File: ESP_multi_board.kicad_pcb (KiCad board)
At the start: 2 copper layers, 23 parts, among them P101 CONN_01X02, P102 CONN_01X06, P103 CONN_01X02, P104 CONN_01X06, P105 CONN_01X12, P106 CONN_01X03, P107 JUMPER1, P108 CONN_I2C_MPU6050, P109 CONN_01X03, P110 CONN_01X03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

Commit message: pendiente de enrutar, TODO: incluir diodos baterias, meditar los jumpers
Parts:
- moved P107 68.6 mm to (118.1, 71.1)
- moved P112 44.6 mm to (113.0, 94.0), turned to 0 degrees
- moved U1 38.6 mm to (134.6, 82.5)
- moved P110 31.4 mm to (168.9, 90.2), turned to 90 degrees
- moved P109 31.4 mm to (165.1, 95.2), turned to 180 degrees
- moved R104 16.9 mm to (160.0, 88.9), turned to 270 degrees
- moved C1 16.6 mm to (154.9, 88.9), turned to 180 degrees
- moved P103 13.1 mm to (151.1, 86.4), turned to 180 degrees
- moved U101 10.8 mm to (154.9, 97.8)
- moved C2 8.98 mm to (154.9, 108.0), turned to 180 degrees
- moved P104 8.52 mm to (194.3, 90.2)
- moved P105 8.13 mm to (146.1, 104.1)
- moved U103 5.68 mm to (125.7, 96.5)
- moved P101 5.24 mm to (157.5, 83.8)
- moved P111 5.24 mm to (190.5, 104.1)
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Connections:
- U103 pad 10: Net-(P105-Pad3) -> Net-(P105-Pad2)
- U103 pad 11: Net-(P105-Pad2) -> Net-(P105-Pad3)
- U103 pad 12: Net-(P105-Pad1) -> Net-(P105-Pad4)
- U103 pad 9: Net-(P105-Pad4) -> Net-(P105-Pad1)
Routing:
- net VDD: track 54.9 -> 11.8 mm
- net Net-(P111-Pad3): track 31.2 -> 0.00 mm
- net Net-(P111-Pad8): track 18.3 -> 0.00 mm
- net Net-(P111-Pad7): track 17.7 -> 0.00 mm
- net Net-(P111-Pad6): track 17.2 -> 0.00 mm
- net Net-(P111-Pad5): track 16.7 -> 0.00 mm
- net Net-(P111-Pad4): track 16.1 -> 0.00 mm
- net ENC2_B: track 13.3 -> 0.00 mm

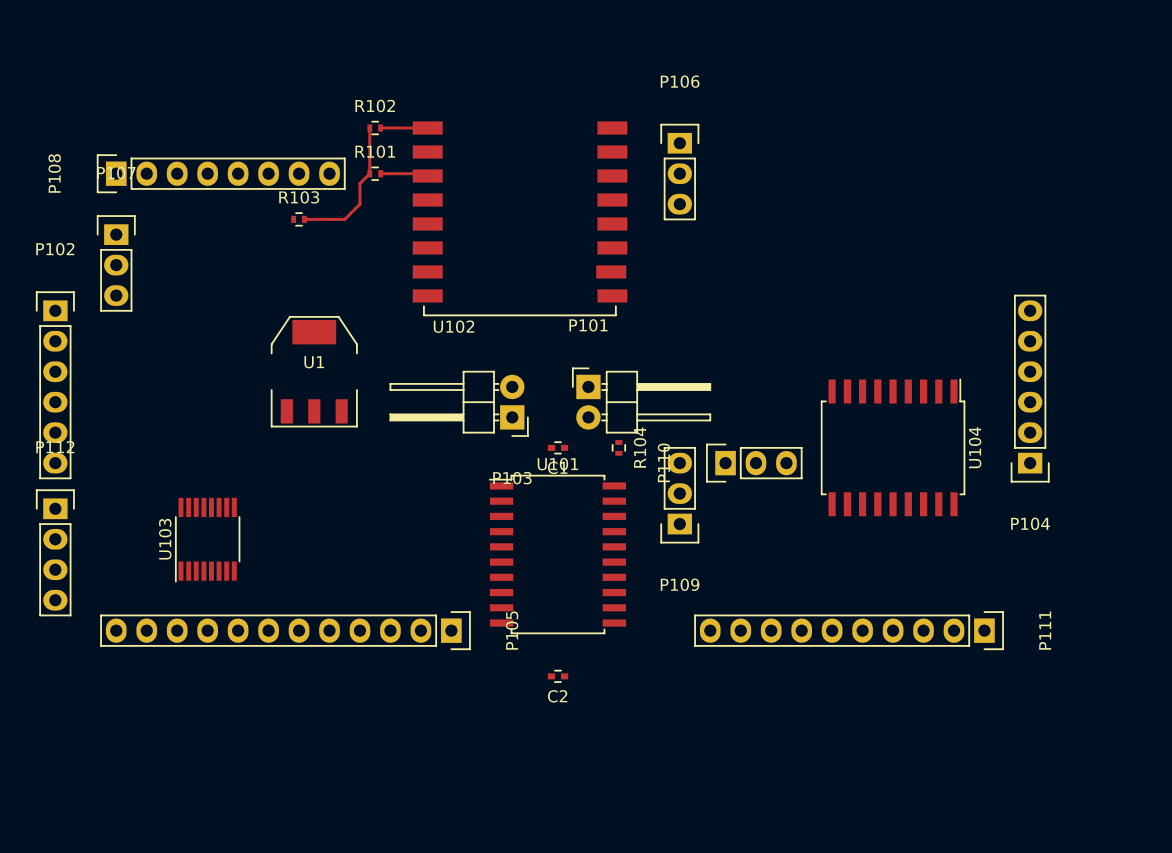
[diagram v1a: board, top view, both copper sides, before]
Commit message: actualizaciones en CRM. TODO: cambiar L293DD por L298smd, cambiar para controlar ENs con pwm, y pines de direccion de motores desde el extensor de pines, eliminar jumpers, ajustar tamaño de las resistencias
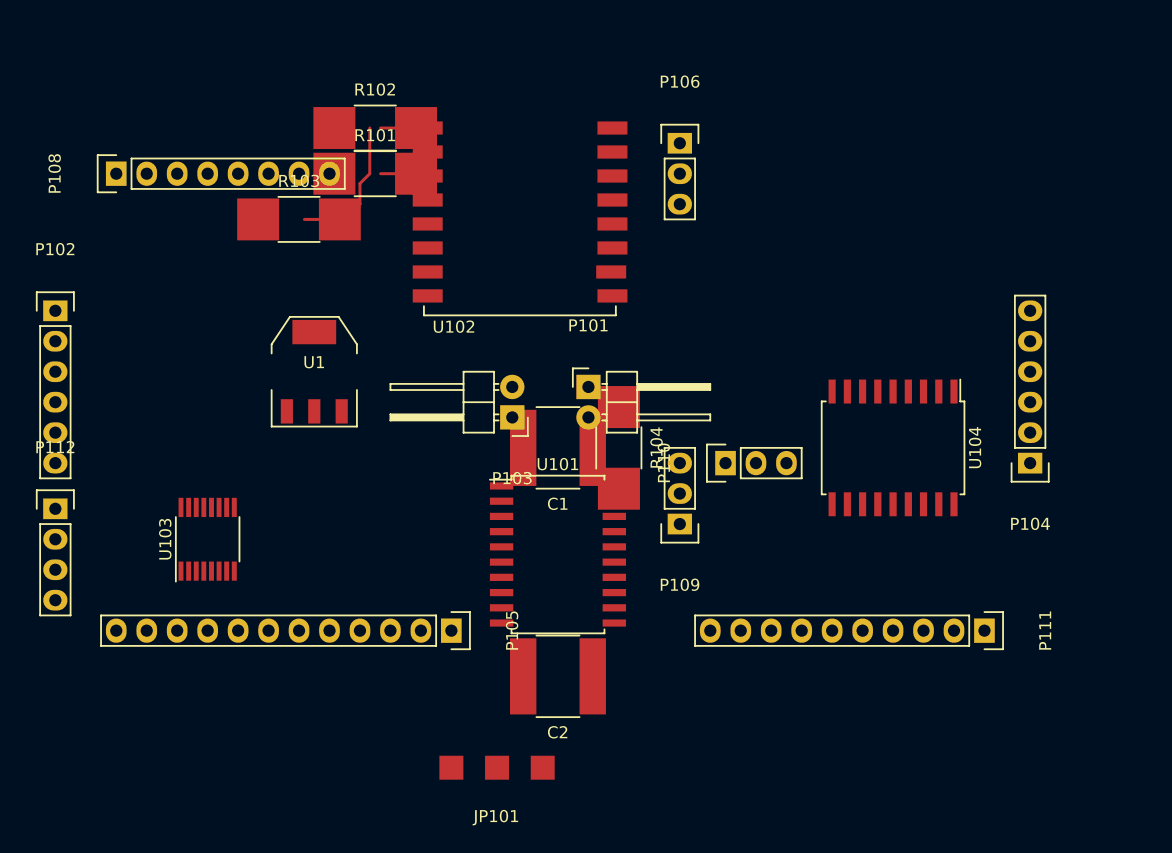
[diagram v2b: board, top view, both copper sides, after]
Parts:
- removed P107: JUMPER1, Pin_Headers:Pin_Header_Straight_1x03
- added JP101: JUMPER3, Oddities:NetTie-II_SMD, F.Cu at (149.9, 115.6)
- C1, C2: footprint Capacitors_SMD:C_0402 -> Capacitors_SMD:C_1825_HandSoldering
- R101, R102, R103, R104: footprint Resistors_SMD:R_0402 -> Resistors_SMD:R_1812_HandSoldering
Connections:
- P108 pad 3: XCL -> (no net)
- P108 pad 4: XDA -> (no net)
- U102 pad 2: AinRaw -> (no net)
- U104 pad 7: Net-(U104-Pad7) -> (no net)

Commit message: modificada huella del jumper, incluidos condensadores en la linea de 3.3v
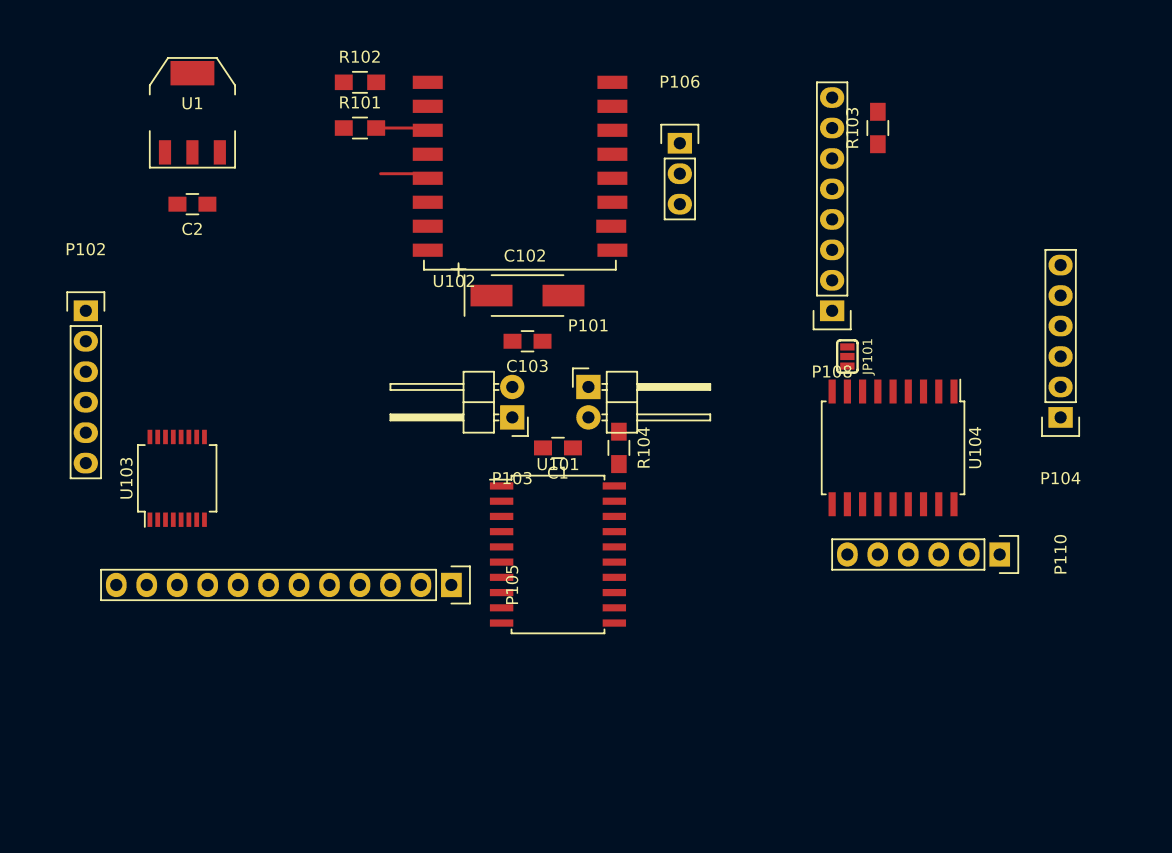
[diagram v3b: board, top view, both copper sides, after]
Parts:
- removed P109: CONN_01X03, Pin_Headers:Pin_Header_Straight_1x03
- removed P111: CONN_DIGITAL, Pin_Headers:Pin_Header_Straight_1x10
- removed P112: CONN_I2C, Pin_Headers:Pin_Header_Straight_1x04
- added C102: 10u, Capacitors_Tantalum_SMD:TantalC_SizeC_EIA-6032_HandSoldering, F.Cu at (152.4, 76.2)
- added C103: 0.1u, Capacitors_SMD:C_0805_HandSoldering, F.Cu at (152.4, 80.0)
- C1, C2: footprint Capacitors_SMD:C_1825_HandSoldering -> Capacitors_SMD:C_0805_HandSoldering
- JP101: footprint Oddities:NetTie-II_SMD -> keyboard_parts:SOLDER_JUMPER_3
- P110: value CONN_01X03 -> CONN_PINES_DIG; footprint Pin_Headers:Pin_Header_Straight_1x03 -> Pin_Headers:Pin_Header_Straight_1x06
- R101, R102, R103, R104: footprint Resistors_SMD:R_1812_HandSoldering -> Resistors_SMD:R_0805_HandSoldering
- U103: footprint Housings_SSOP:QSOP-16_3.9x4.9mm_Pitch0.635mm -> Housings_SSOP:SSOP-16_5.3x6.2mm_Pitch0.65mm
- moved P108 60.8 mm to (177.8, 77.5), turned to 180 degrees
- moved C2 49.8 mm to (124.5, 68.6)
- moved R103 48.9 mm to (181.6, 62.2), turned to 90 degrees
- moved JP101 45.0 mm to (179.1, 81.3), turned to 270 degrees
- moved P110 24.1 mm to (191.8, 97.8), turned to 270 degrees
- moved U1 23.9 mm to (124.5, 61.0)
- moved U103 5.68 mm to (123.2, 91.4)
- moved P104 4.58 mm to (196.8, 86.4)
- moved R101 4.02 mm to (138.4, 62.2)
- moved R102 4.02 mm to (138.4, 58.4)
- moved P105 3.81 mm to (146.1, 100.3)
- moved U102 3.81 mm to (144.8, 58.4)
- moved P102 2.54 mm to (115.6, 77.5)
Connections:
- P110 pad 1: Net-(P110-Pad1) -> GND
- P110 pad 2: Net-(P110-Pad2) -> VDD
- P110 pad 3: ENC2_B -> Net-(P110-Pad3)
- U101 pad 1: VDD -> EN1
- U101 pad 11: VDD -> EN2
- U102 pad 4: M1_A -> EN1
- U102 pad 5: M1_B -> EN2
- U102 pad 6: M2_A -> ENC1_B
- U102 pad 7: M2_B -> ENC2_B
- U104 pad 10: Net-(P109-Pad2) -> M1_A
- U104 pad 11: Net-(P110-Pad2) -> M1_B
- U104 pad 12: Net-(P111-Pad8) -> M2_A
- U104 pad 13: Net-(P111-Pad7) -> M2_B
- U104 pad 14: Net-(P111-Pad6) -> Net-(P110-Pad6)
- U104 pad 15: Net-(P111-Pad5) -> Net-(P110-Pad5)
- U104 pad 16: Net-(P111-Pad4) -> Net-(P110-Pad4)
- U104 pad 17: Net-(P111-Pad3) -> Net-(P110-Pad3)
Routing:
- net VDD: track 11.8 -> 0.00 mm
- net EN2: track 0.00 -> 4.71 mm
- net Net-(R102-Pad2): track 4.63 -> 0.00 mm

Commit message: autorouting generado con freerouting
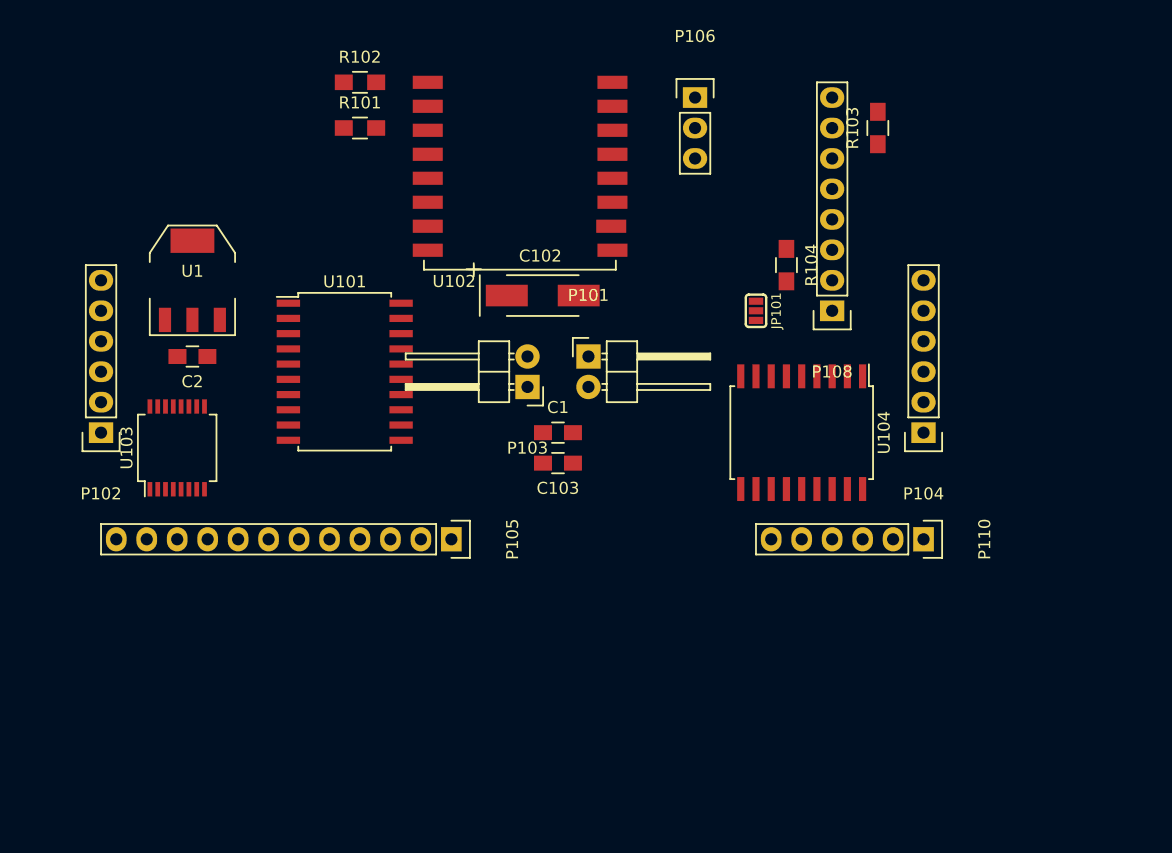
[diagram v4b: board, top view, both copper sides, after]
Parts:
- moved U101 23.4 mm to (137.2, 82.5)
- moved R104 20.7 mm to (174.0, 73.7)
- moved U1 14.0 mm to (124.5, 74.9)
- moved C2 12.7 mm to (124.5, 81.3)
- moved P104 11.5 mm to (185.4, 87.6)
- moved C103 10.5 mm to (154.9, 90.2)
- moved P102 10.2 mm to (116.8, 87.6), turned to 180 degrees
- moved JP101 8.52 mm to (171.4, 77.5)
- moved U104 7.73 mm to (175.3, 87.6)
- moved P110 6.48 mm to (185.4, 96.5)
- moved P106 4.02 mm to (166.4, 59.7)
- moved P105 3.81 mm to (146.1, 96.5)
- moved P103 2.84 mm to (152.4, 83.8)
- moved P101 2.54 mm to (157.5, 81.3)
- moved U103 2.54 mm to (123.2, 88.9)
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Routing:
- net Net-(R101-Pad2): track 4.63 -> 0.00 mm
- net EN2: track 4.71 -> 0.27 mm
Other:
- net class power added: clearance 0.3, trace_width 0.5, via_dia 0.8, via_drill 0.4
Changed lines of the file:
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@@
   (general
     (links 90)
-    (no_connects 89)
-    (area 0 0 0 0)
+    (no_connects 90)
+    (area 111.631667 49.344999 191.595 103.156904)
     (thickness 1.6)
     (drawings 0)
-    (tracks 3)
+    (tracks 1)
     (zones 0)
     (modules 22)
@@
     (add_net ENC2_A)
     (add_net ENC2_B)
-    (add_net GND)
     (add_net GPIO0)
     (add_net M1+)
@@
     (add_net SDA)
     (add_net TX)
+  )
+  (net_class power ""
+    (clearance 0.3)
+    (trace_width 0.5)
+    (via_dia 0.8)
+    (via_drill 0.4)
+    (uvia_dia 0.3)
+    (uvia_drill 0.1)
+    (add_net GND)
     (add_net VCC)
     (add_net VDD)
   )
   (module Pin_Headers:Pin_Header_Angled_1x02 (layer F.Cu)
-    (at 157.48 83.82)
+    (at 157.48 81.28)
     (descr "Through hole pin header")
     (tags "pin header")
@@
   )
   (module Pin_Headers:Pin_Header_Straight_1x06 (layer F.Cu)
-    (at 115.57 77.47)
+    (at 116.84 87.63 180)
     (descr "Through hole pin header")
     (tags "pin header")
-    (fp_text reference P102 (at 0 -5.1) (layer F.SilkS)
-      (effects (font (size 1 1) (thickness 0.15)))
-    )
-    (fp_text value CONN_01X06 (at 0 -3.1) (layer F.Fab)
+    (fp_text reference P102 (at 0 -5.1 180) (layer F.SilkS)
+      (effects (font (size 1 1) (thickness 0.15)))
+    )
+    (fp_text value CONN_01X06 (at 0 -3.1 180) (layer F.Fab)
       (effects (font (size 1 1) (thickness 0.15)))
     )
@@
     (fp_line (start -1.55 0) (end -1.55 -1.55) (layer F.SilkS) (width 0.15))
     (fp_line (start -1.55 -1.55) (end 1.55 -1.55) (layer F.SilkS) (width 0.15))
-    (pad 1 thru_hole rect (at 0 0) (size 2.032 1.7272) (drill 1.016) (layers *.Cu *.Mask F.SilkS)
+    (pad 1 thru_hole rect (at 0 0 180) (size 2.032 1.7272) (drill 1.016) (layers *.Cu *.Mask F.SilkS)
       (net 5 M1+))
-    (pad 2 thru_hole oval (at 0 2.54) (size 2.032 1.7272) (drill 1.016) (layers *.Cu *.Mask F.SilkS)
+    (pad 2 thru_hole oval (at 0 2.54 180) (size 2.032 1.7272) (drill 1.016) (layers *.Cu *.Mask F.SilkS)
       (net 6 M1-))
-    (pad 3 thru_hole oval (at 0 5.08) (size 2.032 1.7272) (drill 1.016) (layers *.Cu *.Mask F.SilkS)
-      (net 1 VDD))
-    (pad 4 thru_hole oval (at 0 7.62) (size 2.032 1.7272) (drill 1.016) (layers *.Cu *.Mask F.SilkS)
-      (net 2 GND))
-    (pad 5 thru_hole oval (at 0 10.16) (size 2.032 1.7272) (drill 1.016) (layers *.Cu *.Mask F.SilkS)
+    (pad 3 thru_hole oval (at 0 5.08 180) (size 2.032 1.7272) (drill 1.016) (layers *.Cu *.Mask F.SilkS)
+      (net 1 VDD))
+    (pad 4 thru_hole oval (at 0 7.62 180) (size 2.032 1.7272) (drill 1.016) (layers *.Cu *.Mask F.SilkS)
+      (net 2 GND))
+    (pad 5 thru_hole oval (at 0 10.16 180) (size 2.032 1.7272) (drill 1.016) (layers *.Cu *.Mask F.SilkS)
       (net 7 ENC1_A))
-    (pad 6 thru_hole oval (at 0 12.7) (size 2.032 1.7272) (drill 1.016) (layers *.Cu *.Mask F.SilkS)
+    (pad 6 thru_hole oval (at 0 12.7 180) (size 2.032 1.7272) (drill 1.016) (layers *.Cu *.Mask F.SilkS)
       (net 8 ENC1_B))
     (model Pin_Headers.3dshapes/Pin_Header_Straight_1x06.wrl
@@
   )
   (module Pin_Headers:Pin_Header_Angled_1x02 (layer F.Cu)
-    (at 151.13 86.36 180)
+    (at 152.4 83.82 180)
     (descr "Through hole pin header")
     (tags "pin header")
@@
   )
   (module Pin_Headers:Pin_Header_Straight_1x06 (layer F.Cu)
-    (at 196.85 86.36 180)
+    (at 185.42 87.63 180)
     (descr "Through hole pin header")
     (tags "pin header")
@@
   )
   (module Pin_Headers:Pin_Header_Straight_1x12 (layer F.Cu)
-    (at 146.05 100.33 270)
+    (at 146.05 96.52 270)
     (descr "Through hole pin header")
     (tags "pin header")
@@
   )
   (module Pin_Headers:Pin_Header_Straight_1x03 (layer F.Cu)
-    (at 165.1 63.5)
+    (at 166.37 59.69)
     (descr "Through hole pin header")
     (tags "pin header")
@@
   )
   (module TO_SOT_Packages_SMD:SOT-223 (layer F.Cu)
-    (at 124.46 60.96)
+    (at 124.46 74.93)
     (descr "module CMS SOT223 4 pins")
     (tags "CMS SOT")
@@
   )
   (module Housings_SOIC:SOIC-20_7.5x12.8mm_Pitch1.27mm (layer F.Cu)
-    (at 154.94 97.79)
+    (at 137.16 82.55)
     (descr "20-Lead Plastic Small Outline (SO) - Wide, 7.50 mm Body [SOIC] (see Microchip Packaging Specification 00000049BS.pdf)")
     (tags "SOIC 1.27")
@@
   )
   (module Housings_SOIC:SOIC-18_7.5x11.6mm_Pitch1.27mm (layer F.Cu)
-    (at 182.88 88.9 270)
+    (at 175.26 87.63 270)
     (descr "18-Lead Plastic Small Outline (SO) - Wide, 7.50 mm Body [SOIC] (see Microchip Packaging Specification 00000049BS.pdf)")
     (tags "SOIC 1.27")
@@
   )
   (module Pin_Headers:Pin_Header_Straight_1x06 (layer F.Cu)
-    (at 191.77 97.79 270)
+    (at 185.42 96.52 270)
     (descr "Through hole pin header")
     (tags "pin header")
@@
   )
   (module Housings_SSOP:SSOP-16_5.3x6.2mm_Pitch0.65mm (layer F.Cu)
-    (at 123.19 91.44 90)
+    (at 123.19 88.9 90)
     (descr "SSOP16: plastic shrink small outline package; 16 leads; body width 5.3 mm; (see NXP SSOP-TSSOP-VSO-REFLOW.pdf and sot338-1_po.pdf)")
     (tags "SSOP 0.65")
@@
   )
   (module Capacitors_SMD:C_0805_HandSoldering (layer F.Cu)
-    (at 154.94 88.9 180)
+    (at 154.94 87.63)
     (descr "Capacitor SMD 0805, hand soldering")
     (tags "capacitor 0805")
     (attr smd)
-    (fp_text reference C1 (at 0 -2.1 180) (layer F.SilkS)
-      (effects (font (size 1 1) (thickness 0.15)))
-    )
-    (fp_text value 10u (at 0 2.1 180) (layer F.Fab)
+    (fp_text reference C1 (at 0 -2.1) (layer F.SilkS)
+      (effects (font (size 1 1) (thickness 0.15)))
+    )
+    (fp_text value 10u (at 0 2.1) (layer F.Fab)
       (effects (font (size 1 1) (thickness 0.15)))
     )
@@
     (fp_line (start 0.5 -0.85) (end -0.5 -0.85) (layer F.SilkS) (width 0.15))
     (fp_line (start -0.5 0.85) (end 0.5 0.85) (layer F.SilkS) (width 0.15))
-    (pad 1 smd rect (at -1.25 0 180) (size 1.5 1.25) (layers F.Cu F.Paste F.Mask)
-      (net 1 VDD))
-    (pad 2 smd rect (at 1.25 0 180) (size 1.5 1.25) (layers F.Cu F.Paste F.Mask)
+    (pad 1 smd rect (at -1.25 0) (size 1.5 1.25) (layers F.Cu F.Paste F.Mask)
+      (net 1 VDD))
+    (pad 2 smd rect (at 1.25 0) (size 1.5 1.25) (layers F.Cu F.Paste F.Mask)
       (net 2 GND))
     (model Capacitors_SMD.3dshapes/C_0805_HandSoldering.wrl
@@
   )
   (module Capacitors_SMD:C_0805_HandSoldering (layer F.Cu)
-    (at 124.46 68.58 180)
+    (at 124.46 81.28 180)
     (descr "Capacitor SMD 0805, hand soldering")
     (tags "capacitor 0805")
@@
   )
   (module Capacitors_Tantalum_SMD:TantalC_SizeC_EIA-6032_HandSoldering (layer F.Cu)
-    (at 152.4 76.2)
+    (at 153.67 76.2)
     (descr "Tantal Cap. , Size C, EIA-6032, Hand Soldering,")
     (tags "Tantal Cap. , Size C, EIA-6032, Hand Soldering,")
@@
   )
   (module Capacitors_SMD:C_0805_HandSoldering (layer F.Cu)
-    (at 152.4 80.01 180)
+    (at 154.94 90.17 180)
     (descr "Capacitor SMD 0805, hand soldering")
     (tags "capacitor 0805")
@@
   )
   (module Resistors_SMD:R_0805_HandSoldering (layer F.Cu)
-    (at 160.02 88.9 270)
+    (at 173.99 73.66 270)
     (descr "Resistor SMD 0805, hand soldering")
     (tags "resistor 0805")
@@
   )
   (module keyboard_parts:SOLDER_JUMPER_3 (layer F.Cu)
-    (at 179.07 81.28 270)
+    (at 171.45 77.47 270)
     (tags "solder jumper bridge configuration")
     (attr virtual)
@@
       (net 36 "Net-(JP101-Pad1)") (clearance 0.1))
   )
-  (segment (start 144.78 62.23) (end 140.15 62.23) (width 0.25) (layer F.Cu) (net 30) (status 30))
-  (segment (start 140.15 66.04) (end 144.59 66.04) (width 0.25) (layer F.Cu) (net 43) (status 30))
   (segment (start 144.59 66.04) (end 144.78 66.23) (width 0.25) (layer F.Cu) (net 43) (status 30))
 )
